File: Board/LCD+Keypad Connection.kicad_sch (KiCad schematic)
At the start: 5 parts, among them CN2 TO BOARD's CN3, CN4 TO BOARD's CN1, U1 LCD HD44780, U2 KEYPAD NUMERIC 3x4

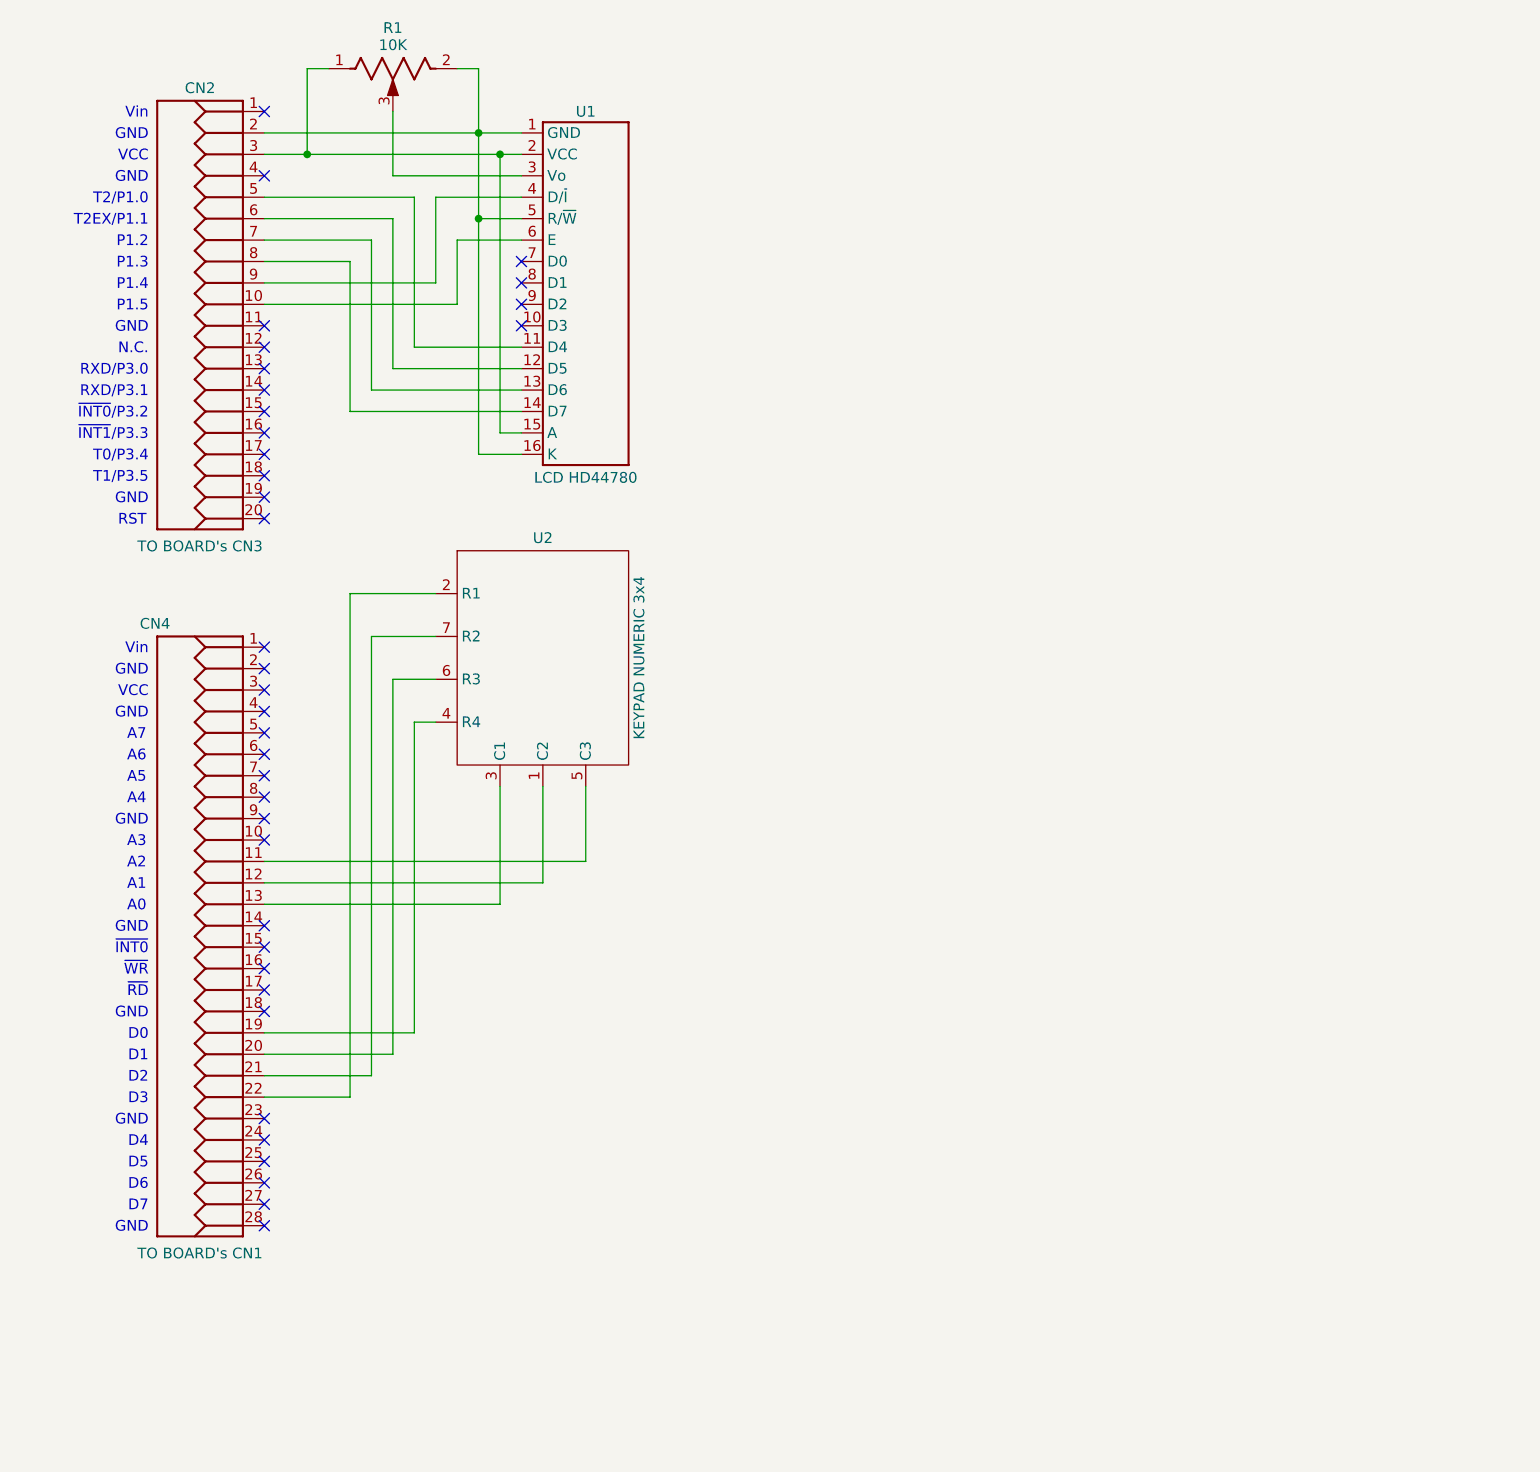
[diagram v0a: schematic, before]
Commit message: Added PDF files with the schematics.
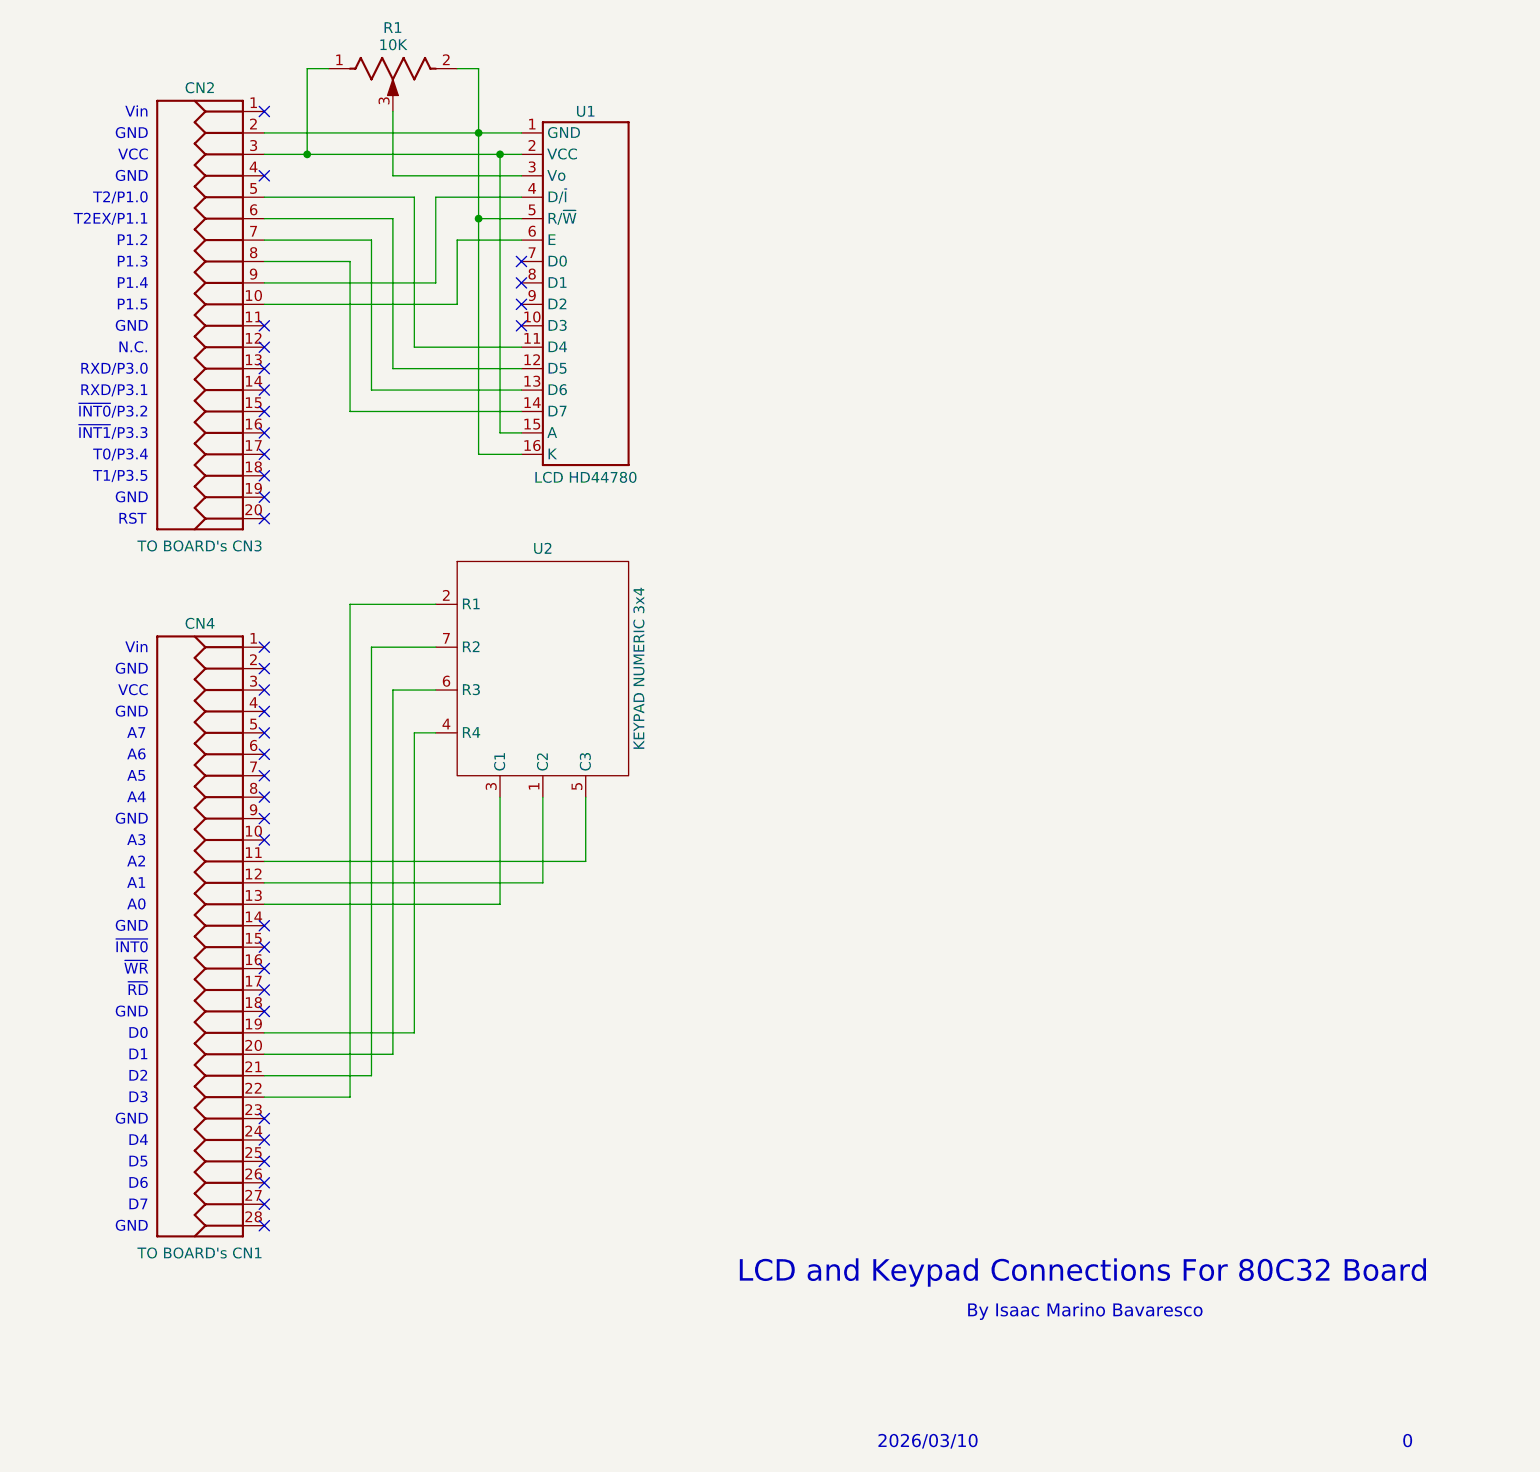
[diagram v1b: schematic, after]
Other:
- note added: "0"
- note added: "2026/03/10"
- note added: "By Isaac Marino Bavaresco"
- note added: "LCD and Keypad Connections For 80C32 Board"
- moved on the sheet: U2
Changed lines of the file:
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@@
+		)
+	)
+	(text "0"
+		(exclude_from_sim no)
+		(at 269.494 194.31 0)
+		(effects
+			(font
+				(size 1.524 1.524)
+			)
+			(justify left bottom)
 		)
 	)
@@
 		)
 	)
+	(text "LCD and Keypad Connections For 80C32 Board"
+		(exclude_from_sim no)
+		(at 231.648 173.228 0)
+		(effects
+			(font
+				(size 2.54 2.54)
+			)
+		)
+	)
 	(text "GND"
 		(exclude_from_sim no)
@@
 		)
 	)
+	(text "By Isaac Marino Bavaresco"
+		(exclude_from_sim no)
+		(at 231.902 178.816 0)
+		(effects
+			(font
+				(size 1.524 1.524)
+			)
+			(justify bottom)
+		)
+	)
 	(text "D4"
 		(exclude_from_sim no)
@@
 			)
 			(justify right)
+		)
+	)
+	(text "2026/03/10"
+		(exclude_from_sim no)
+		(at 207.264 194.31 0)
+		(effects
+			(font
+				(size 1.524 1.524)
+			)
+			(justify left bottom)
 		)
 	)
@@
 	(wire
 		(pts
-			(xy 167.64 115.57) (xy 167.64 127)
+			(xy 167.64 116.84) (xy 167.64 127)
 		)
 		(stroke
@@
 	(wire
 		(pts
-			(xy 152.4 107.95) (xy 154.94 107.95)
+			(xy 152.4 109.22) (xy 154.94 109.22)
 		)
 		(stroke
@@
 	(wire
 		(pts
-			(xy 154.94 92.71) (xy 144.78 92.71)
-		)
-		(stroke
-			(width 0)
-			(type default)
-		)
-	)
-	(wire
-		(pts
-			(xy 149.86 102.87) (xy 149.86 147.32)
-		)
-		(stroke
-			(width 0)
-			(type default)
-		)
-	)
-	(wire
-		(pts
-			(xy 162.56 115.57) (xy 162.56 129.54)
+			(xy 154.94 93.98) (xy 144.78 93.98)
+		)
+		(stroke
+			(width 0)
+			(type default)
+		)
+	)
+	(wire
+		(pts
+			(xy 149.86 104.14) (xy 149.86 147.32)
+		)
+		(stroke
+			(width 0)
+			(type default)
+		)
+	)
+	(wire
+		(pts
+			(xy 162.56 116.84) (xy 162.56 129.54)
 		)
 		(stroke
@@
 	(wire
 		(pts
-			(xy 172.72 115.57) (xy 172.72 124.46)
+			(xy 172.72 116.84) (xy 172.72 124.46)
 		)
 		(stroke
@@
 	(wire
 		(pts
-			(xy 152.4 144.78) (xy 152.4 107.95)
-		)
-		(stroke
-			(width 0)
-			(type default)
-		)
-	)
-	(wire
-		(pts
-			(xy 147.32 97.79) (xy 147.32 149.86)
+			(xy 152.4 144.78) (xy 152.4 109.22)
+		)
+		(stroke
+			(width 0)
+			(type default)
+		)
+	)
+	(wire
+		(pts
+			(xy 147.32 99.06) (xy 147.32 149.86)
 		)
 		(stroke
@@
 	(wire
 		(pts
-			(xy 144.78 92.71) (xy 144.78 152.4)
-		)
-		(stroke
-			(width 0)
-			(type default)
-		)
-	)
-	(wire
-		(pts
-			(xy 154.94 97.79) (xy 147.32 97.79)
+			(xy 144.78 93.98) (xy 144.78 152.4)
+		)
+		(stroke
+			(width 0)
+			(type default)
+		)
+	)
+	(wire
+		(pts
+			(xy 154.94 99.06) (xy 147.32 99.06)
 		)
 		(stroke
@@
 	(wire
 		(pts
-			(xy 154.94 102.87) (xy 149.86 102.87)
+			(xy 154.94 104.14) (xy 149.86 104.14)
 		)
 		(stroke
@@
 		(dnp no)
 		(property "Reference" "CN4"
-			(at 121.666 97.028 0)
+			(at 127 97.028 0)
 			(effects
 				(font
@@
 	(symbol
 		(lib_id "80C32-3:KEYPAD-3X4")
-		(at 154.94 92.71 0)
+		(at 154.94 93.98 0)
 		(unit 1)
 		(exclude_from_sim no)
@@
 		(dnp no)
 		(property "Reference" "U2"
-			(at 167.64 86.868 0)
+			(at 167.64 88.138 0)
 			(effects
 				(font
@@
 		)
 		(property "Value" "KEYPAD NUMERIC 3x4"
-			(at 179.07 100.33 90)
+			(at 179.07 101.6 90)
 			(effects
 				(font
@@
 		)
 		(property "Footprint" ""
-			(at 154.94 92.71 0)
+			(at 154.94 93.98 0)
 			(effects
 				(font
@@
 		)
 		(property "Datasheet" ""
-			(at 154.94 92.71 0)
+			(at 154.94 93.98 0)
 			(effects
 				(font
@@
 		)
 		(property "Description" ""
-			(at 154.94 92.71 0)
-			(effects
-				(font
+			(at 154.94 93.98 0)
+			(effects
+				(font
